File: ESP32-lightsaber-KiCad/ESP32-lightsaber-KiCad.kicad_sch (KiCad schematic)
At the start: 7 parts, among them J1 Conn_01x05, SW1 SW_Push

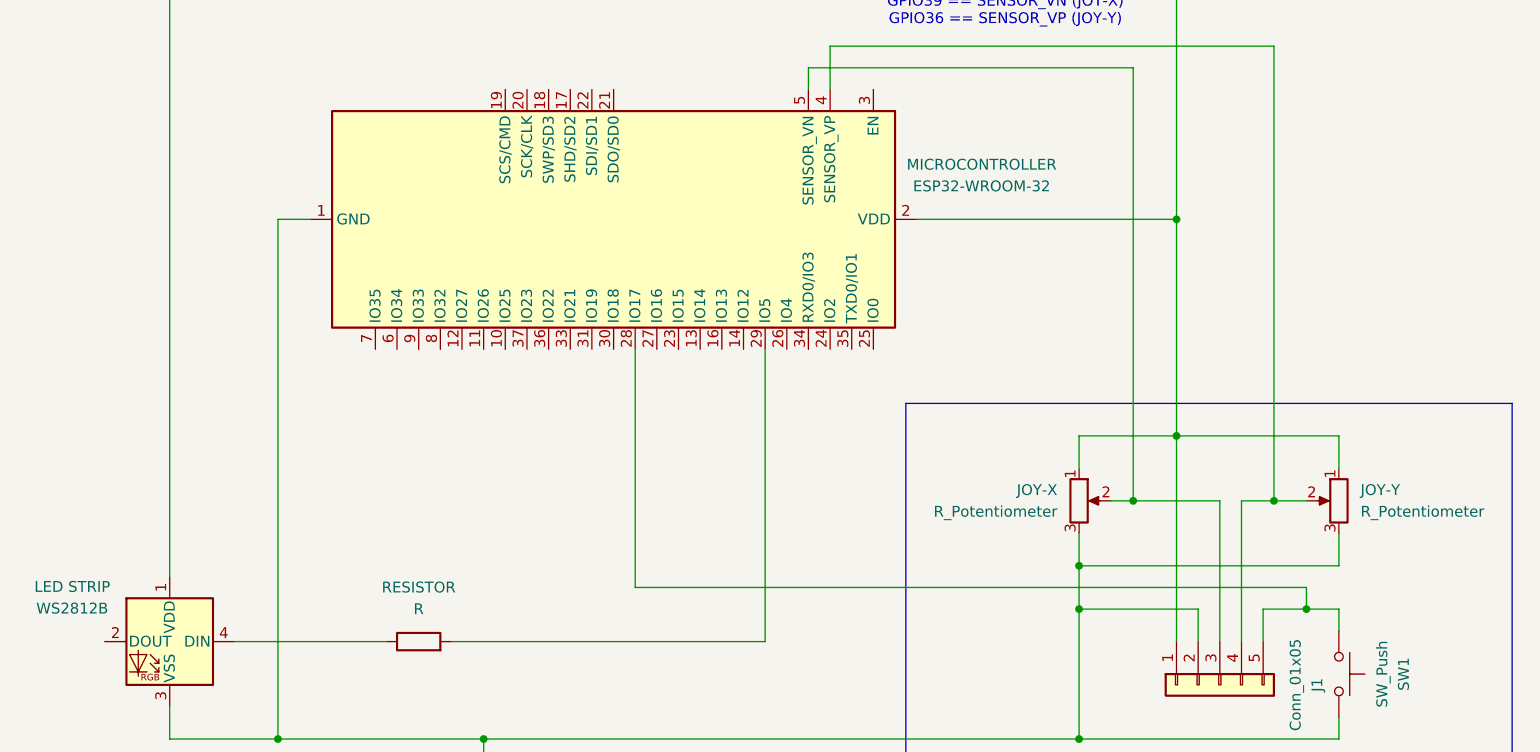
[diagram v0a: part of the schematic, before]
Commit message: Drafted PCB prototype in KiCad from schematic
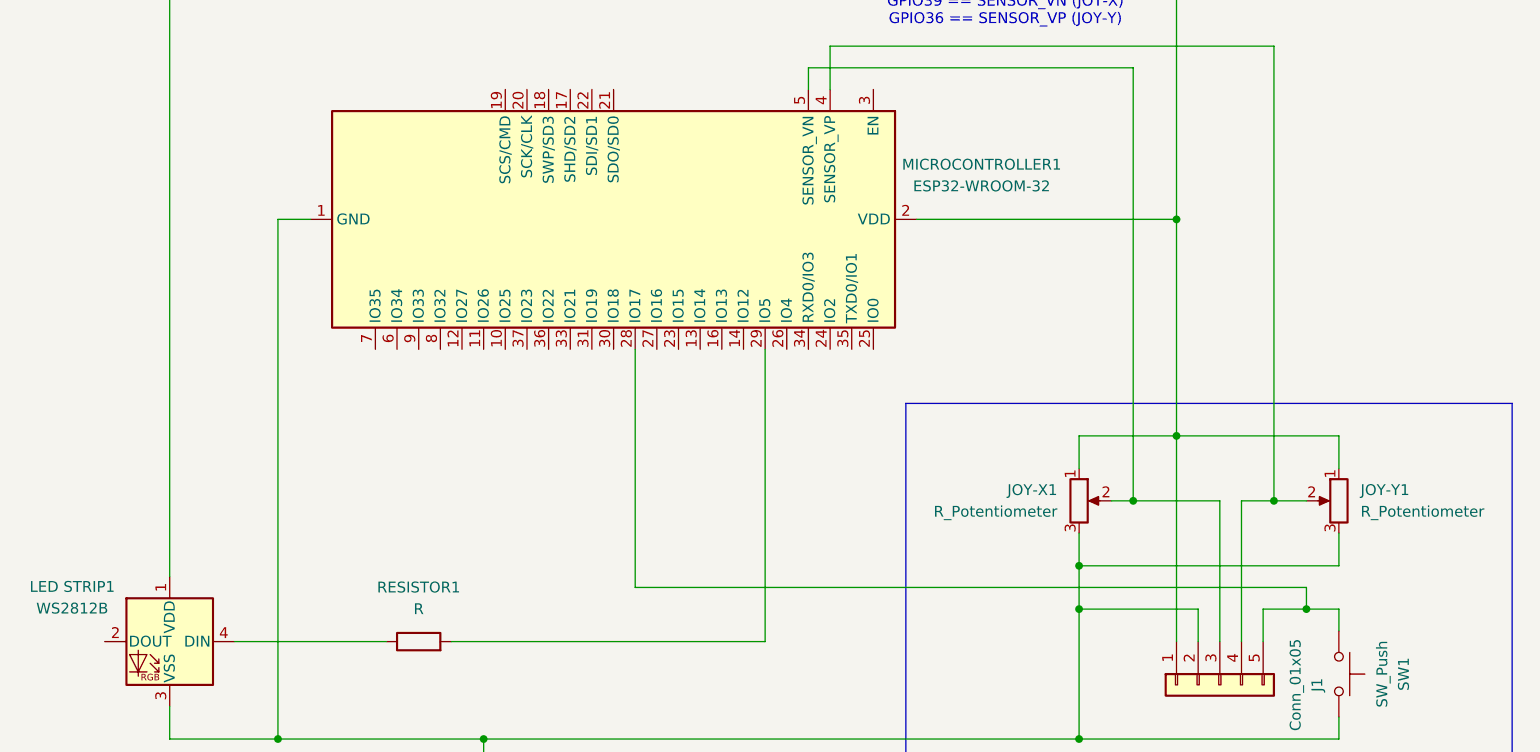
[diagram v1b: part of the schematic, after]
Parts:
- J1: footprint (none) -> Connector_PinHeader_2.54mm:PinHeader_1x05_P2.54mm_Vertical
- JOY-X1: renamed from JOY-X; footprint (none) -> Potentiometer_THT:Potentiometer_Bourns_3386P_Vertical
- JOY-Y1: renamed from JOY-Y; footprint (none) -> Potentiometer_THT:Potentiometer_Bourns_3386P_Vertical
- LED STRIP1: renamed from LED STRIP
- RESISTOR1: renamed from RESISTOR; footprint (none) -> Resistor_SMD:R_0805_2012Metric
- SW1: footprint (none) -> Button_Switch_THT:SW_PUSH_6mm_H9.5mm
- renumbered MICROCONTROLLER to MICROCONTROLLER1
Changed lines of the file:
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@@
 		(dnp no)
 		(fields_autoplaced yes)
-		(property "Reference" "RESISTOR"
+		(property "Reference" "RESISTOR1"
 			(at 130.81 111.76 90)
 			(effects
@@
 			)
 		)
-		(property "Footprint" ""
+		(property "Footprint" "Resistor_SMD:R_0805_2012Metric"
 			(at 130.81 119.888 90)
 			(effects
@@
 			(project ""
 				(path "/47fd40ea-e063-46a8-8976-a1eadddd5f35"
-					(reference "RESISTOR")
+					(reference "RESISTOR1")
 					(unit 1)
 				)
@@
 		(on_board yes)
 		(dnp no)
-		(property "Reference" "LED STRIP"
+		(property "Reference" "LED STRIP1"
 			(at 90.17 111.6898 0)
 			(effects
@@
 			(project ""
 				(path "/47fd40ea-e063-46a8-8976-a1eadddd5f35"
-					(reference "LED STRIP")
+					(reference "LED STRIP1")
 					(unit 1)
 				)
@@
 		(dnp no)
 		(fields_autoplaced yes)
-		(property "Reference" "JOY-X"
+		(property "Reference" "JOY-X1"
 			(at 205.74 100.3299 0)
 			(effects
@@
 			)
 		)
-		(property "Footprint" ""
+		(property "Footprint" "Potentiometer_THT:Potentiometer_Bourns_3386P_Vertical"
 			(at 208.28 101.6 0)
 			(effects
@@
 			(project ""
 				(path "/47fd40ea-e063-46a8-8976-a1eadddd5f35"
-					(reference "JOY-X")
+					(reference "JOY-X1")
 					(unit 1)
 				)
@@
 		(on_board yes)
 		(dnp no)
-		(property "Reference" "JOY-Y"
+		(property "Reference" "JOY-Y1"
 			(at 241.3 100.3299 0)
 			(effects
@@
 			)
 		)
-		(property "Footprint" ""
+		(property "Footprint" "Potentiometer_THT:Potentiometer_Bourns_3386P_Vertical"
 			(at 238.76 101.6 0)
 			(effects
@@
 			(project ""
 				(path "/47fd40ea-e063-46a8-8976-a1eadddd5f35"
-					(reference "JOY-Y")
+					(reference "JOY-Y1")
 					(unit 1)
 				)
@@
 		(dnp no)
 		(fields_autoplaced yes)
-		(property "Reference" "MICROCONTROLLER"
+		(property "Reference" "MICROCONTROLLER1"
 			(at 196.85 62.1598 90)
 			(effects
@@
 			(project ""
 				(path "/47fd40ea-e063-46a8-8976-a1eadddd5f35"
-					(reference "MICROCONTROLLER")
+					(reference "MICROCONTROLLER1")
 					(unit 1)
 				)
@@
 			)
 		)
-		(property "Footprint" ""
+		(property "Footprint" "Button_Switch_THT:SW_PUSH_6mm_H9.5mm"
 			(at 243.84 121.92 0)
 			(effects
@@
 			)
 		)
-		(property "Footprint" ""
+		(property "Footprint" "Connector_PinHeader_2.54mm:PinHeader_1x05_P2.54mm_Vertical"
 			(at 224.79 123.19 0)
 			(effects

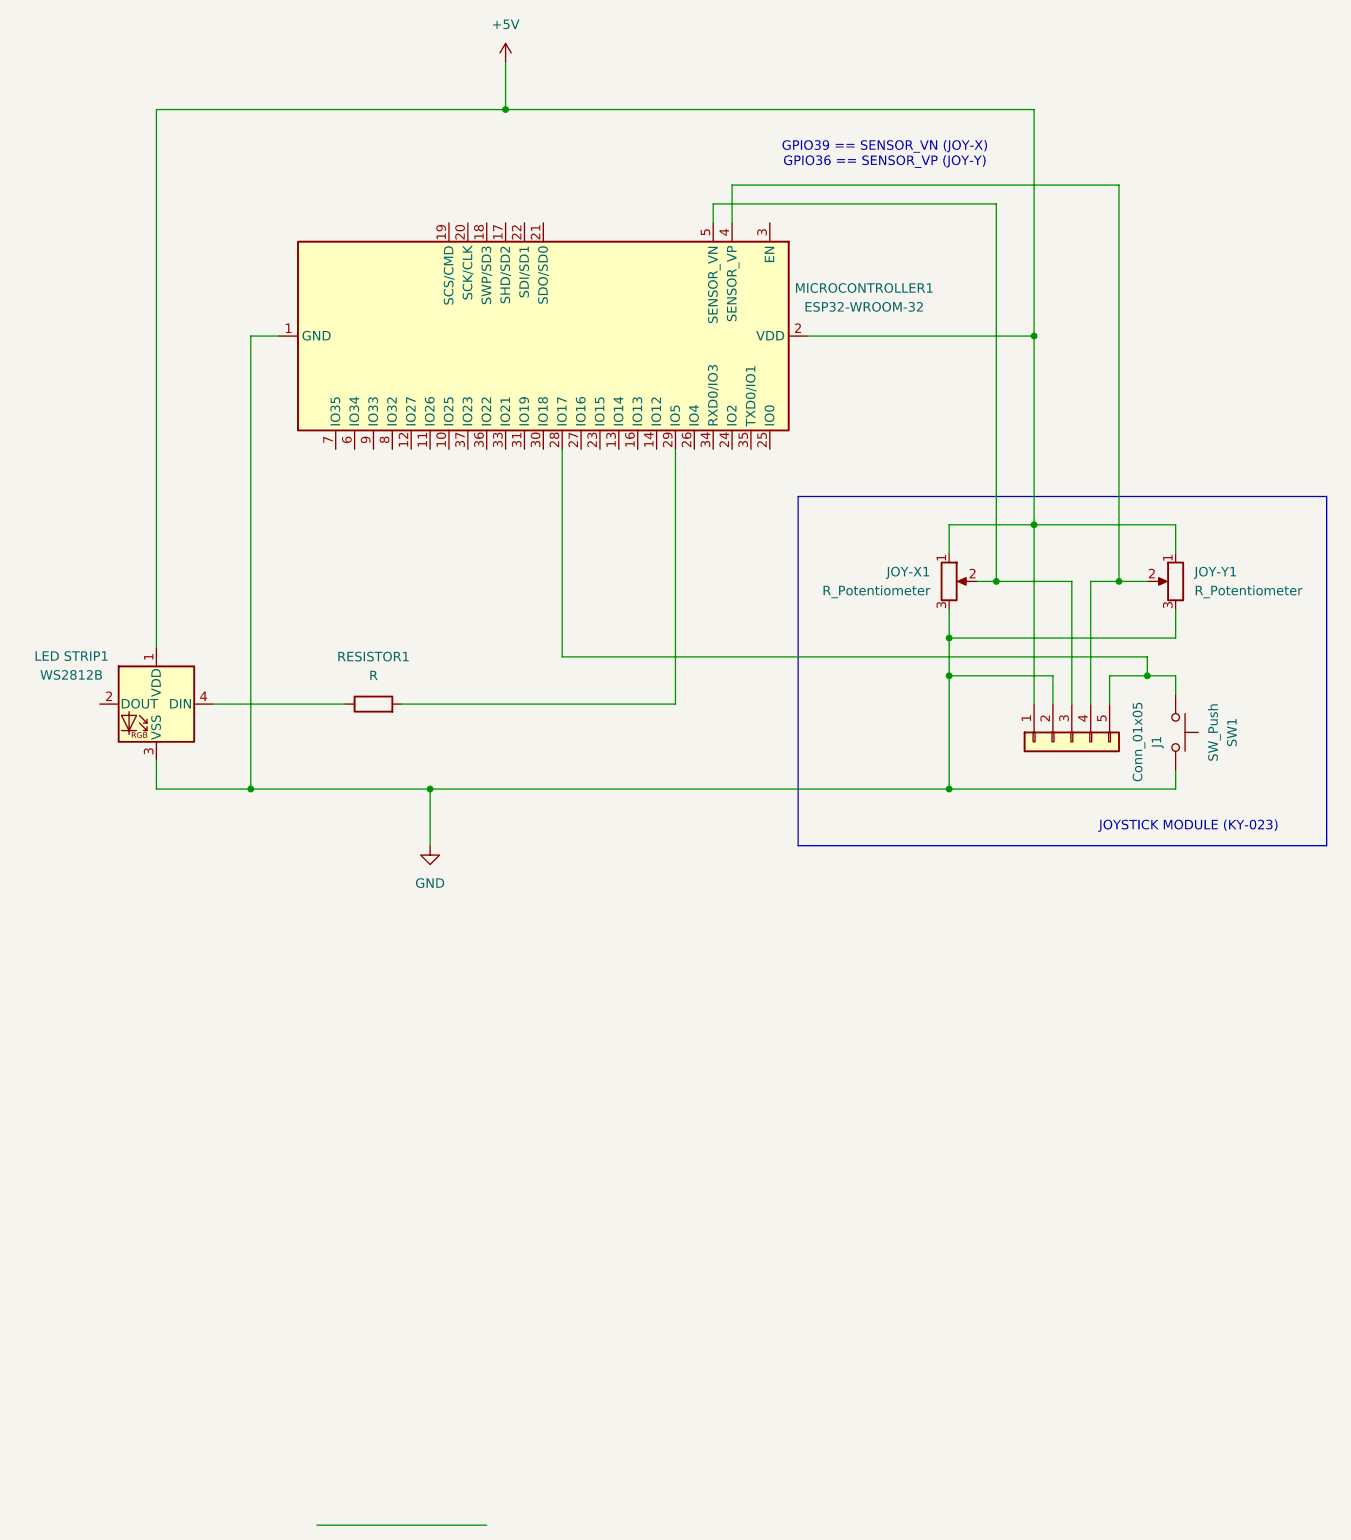
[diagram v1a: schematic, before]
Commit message: Modified lightsaber schematic & PCB following prototype feedback
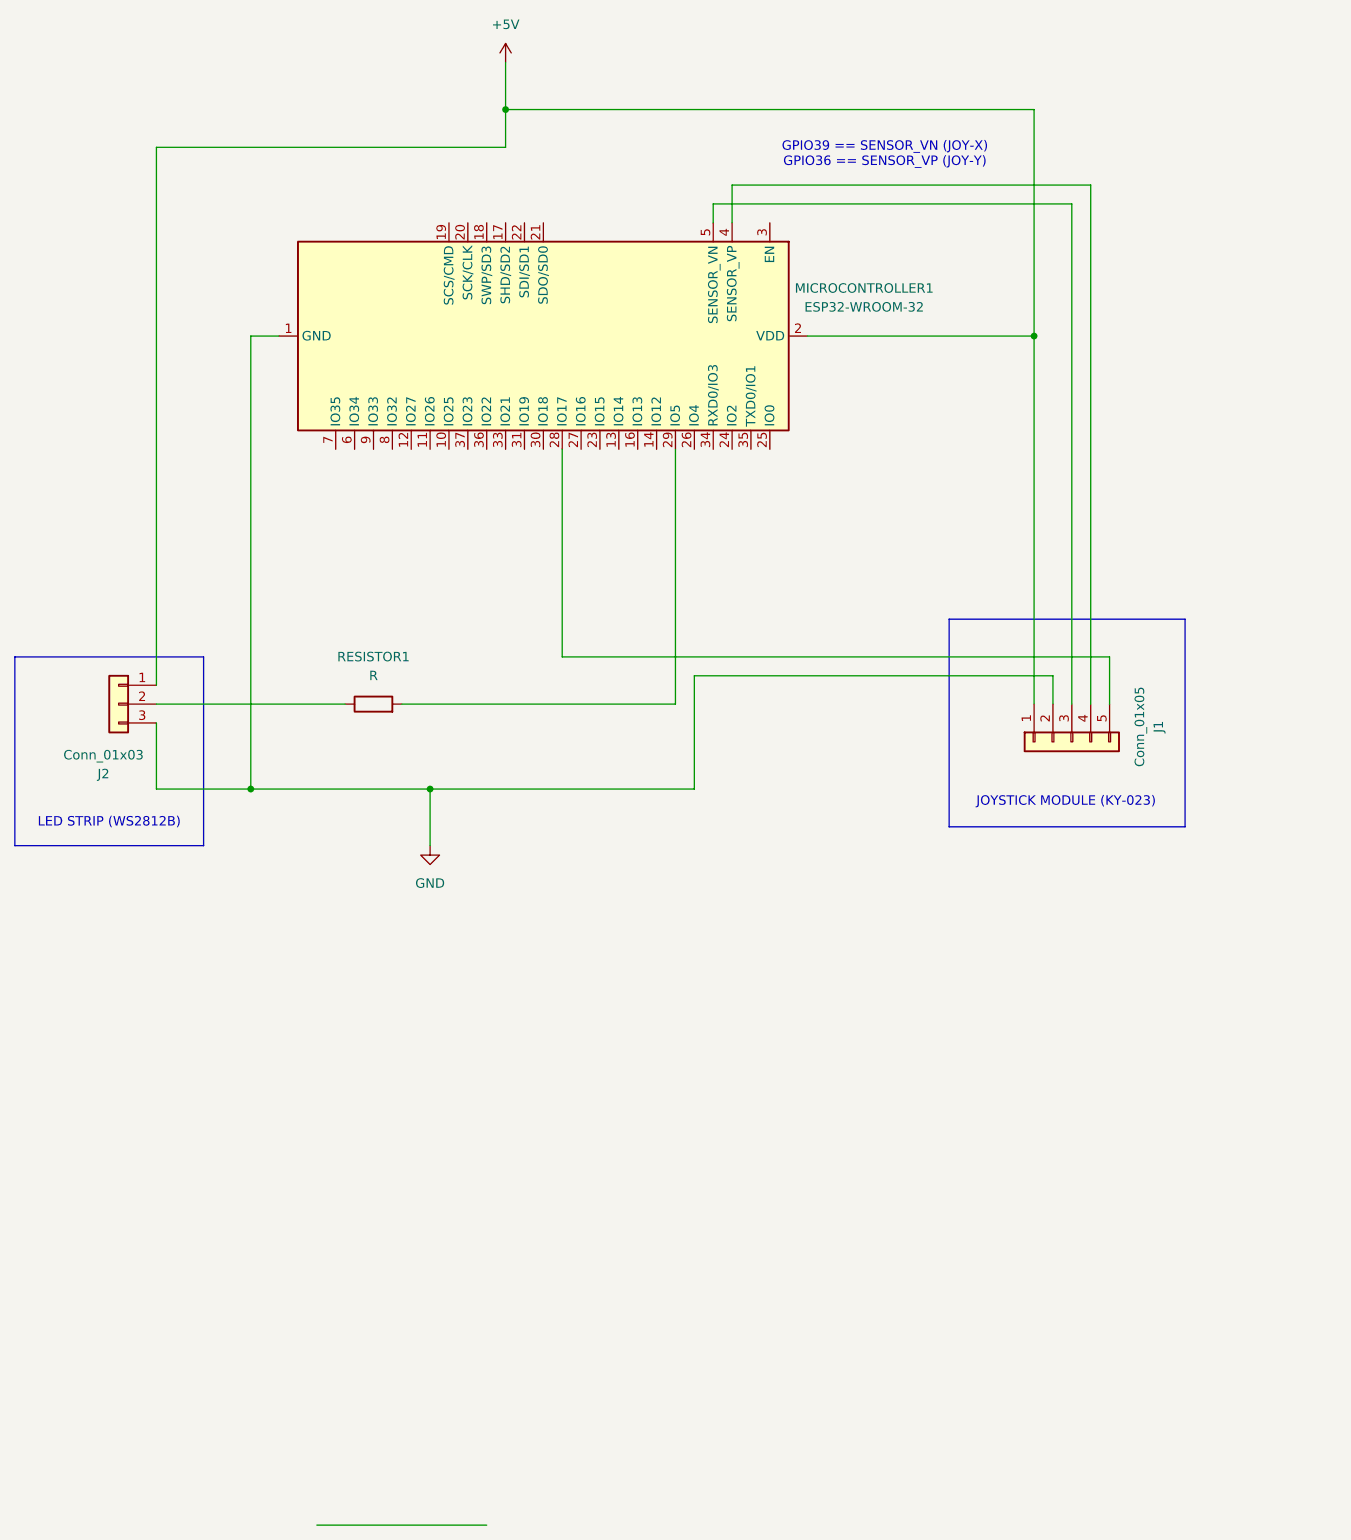
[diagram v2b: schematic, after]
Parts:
- removed JOY-X1, JOY-Y1: R_Potentiometer, Potentiometer_THT:Potentiometer_Bourns_3386P_Vertical, symbol Device:R_Potentiometer
- removed LED STRIP1: WS2812B, LED_SMD:LED_WS2812B_PLCC4_5.0x5.0mm_P3.2mm, symbol LED:WS2812B
- removed SW1: SW_Push, Button_Switch_THT:SW_PUSH_6mm_H9.5mm, symbol Switch:SW_Push
- added J2: Conn_01x03, Connector_PinHeader_2.54mm:PinHeader_1x03_P2.54mm_Vertical, symbol Connector_Generic:Conn_01x03
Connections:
- net +5V: now also J2.1 (Pin_1)
- net GND: now also J2.3 (Pin_3)
- net at RESISTOR1.1: now also J2.2 (Pin_2)
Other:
- note added: "LED STRIP (WS2812B)"
